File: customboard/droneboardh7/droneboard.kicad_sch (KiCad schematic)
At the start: 62 parts, among them J1 Conn_01x04, J10 Conn_01x03_Pin, J2 Conn_01x04, J3 Conn_01x05_Pin, J4 Conn_01x02_Pin, J5 USB_C_Receptacle_USB2.0_16P, J6 Conn_01x04, SW1 SW_Push, SW2 SW_Push, U1 AP62300Z6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

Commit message: stuff
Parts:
- removed J3: Conn_01x05_Pin, Connector_PinHeader_2.00mm:PinHeader_1x05_P2.00mm_Vertical, symbol Connector_Generic:Conn_01x05
- removed J4: Conn_01x02_Pin, Connector_PinHeader_2.54mm:PinHeader_1x02_P2.54mm_Vertical, symbol Connector_Generic:Conn_01x02
- removed R12, R2: 10K, Resistor_SMD:R_0201_0603Metric, symbol Device:R
- added J3, J4: Conn_01x08_MountingPin, Connector_JST:JST_SH_SM08B-SRSS-TB_1x08-1MP_P1.00mm_Horizontal, symbol Connector_Generic_MountingPin:Conn_01x08_MountingPin
- added Q1: DMN2056U, Package_TO_SOT_SMD:SOT-23, symbol Transistor_FET:DMN2056U
- J1, J2, J6: footprint Custom:PinHeaderWide4x -> Connector_JST:JST_SH_SM04B-SRSS-TB_1x04-1MP_P1.00mm_Horizontal; symbol Connector_Generic:Conn_01x04 -> Connector_Generic_MountingPin:Conn_01x04_MountingPin
- SW1, SW2: footprint Button_Switch_THT:SW_PUSH_1P1T_6x3.5mm_H4.3_APEM_MJTP1243 -> Button_Switch_SMD:SW_Push_1P1T-SH_NO_CK_KMR2xxG; symbol Switch:SW_Push -> Switch:SW_Push_Shielded
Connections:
- net 12V: now also J3.1 (Pin_1), J4.2 (Pin_2)
- net GND: now also J1.MP (MountPin), J2.MP (MountPin), J6.MP (MountPin), R1.2, SW1.SH (B), SW2.SH (B), J3.2 (Pin_2), J3.MP (MountPin), J4.1 (Pin_1), J4.MP (MountPin), Q1.2 (S); no longer J2.2 (Pin_2)
- net MOTOR0: now also J3.5 (Pin_5), J4.5 (Pin_5)
- net MOTOR1: now also J3.6 (Pin_6), J4.6 (Pin_6)
- net MOTOR2: now also J3.7 (Pin_7), J4.3 (Pin_3)
- net MOTOR3: now also J3.8 (Pin_8), J4.4 (Pin_4)
- net U4RX: no longer R1.1
- net VMCU: no longer R1.2
- net VTX_PWR: now reaches U3.4 (PE5)
- net VTX_PWR: now also R1.1, Q1.1 (G)
- new net: J2.2 (Pin_2), Q1.3 (D)
- no-connect marks 62 -> 65

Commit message: stuff
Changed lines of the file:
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@@
+	(wire
+		(pts
+			(xy 50.8 80.01) (xy 63.5 80.01)
+		)
+		(stroke
+			(width 0)
+			(type default)
+		)
+	)
 	(wire
 		(pts
@@
 	)
 	(label "VMCU"
-		(at 63.5 80.01 180)
-		(effects
-			(font
-				(size 1.27 1.27)
-			)
-			(justify right bottom)
-		)
-	)
+		(at 50.8 80.01 0)
+		(effects
+			(font
+				(size 1.27 1.27)
+			)
+			(justify left bottom)
+		)
+	)

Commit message: stuff
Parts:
- C10: footprint Capacitor_SMD:C_0402_1005Metric -> Capacitor_SMD:C_0603_1608Metric
- J1, J2, J6: value Conn_01x04 -> Conn_01x04_MountingPin
- SW1, SW2: value SW_Push -> KMR221GLFS
- Y2: value CSTNE20M0V53Z000R0 -> CSTNE8M00G520000R0
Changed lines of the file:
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@@
 			)
 		)
-		(property "Value" "Conn_01x04"
+		(property "Value" "Conn_01x04_MountingPin"
 			(at 80.01 248.0055 0)
 			(effects
@@
 			)
 		)
-		(property "Value" "SW_Push"
+		(property "Value" "KMR221GLFS"
 			(at 64.77 58.42 0)
 			(effects
@@
 			)
 		)
-		(property "Footprint" "Capacitor_SMD:C_0402_1005Metric"
+		(property "Footprint" "Capacitor_SMD:C_0603_1608Metric"
 			(at 124.1552 49.53 0)
 			(effects
@@
 			)
 		)
-		(property "Value" "CSTNE20M0V53Z000R0"
+		(property "Value" "CSTNE8M00G520000R0"
 			(at 39.37 83.8199 90)
 			(effects
@@
 			)
 		)
-		(property "Value" "Conn_01x04"
+		(property "Value" "Conn_01x04_MountingPin"
 			(at 116.84 249.2755 0)
 			(effects
@@
 			)
 		)
-		(property "Value" "Conn_01x04"
+		(property "Value" "Conn_01x04_MountingPin"
 			(at 49.53 248.0055 0)
 			(effects
@@
 			)
 		)
-		(property "Value" "SW_Push"
+		(property "Value" "KMR221GLFS"
 			(at 46.99 57.15 0)
 			(effects

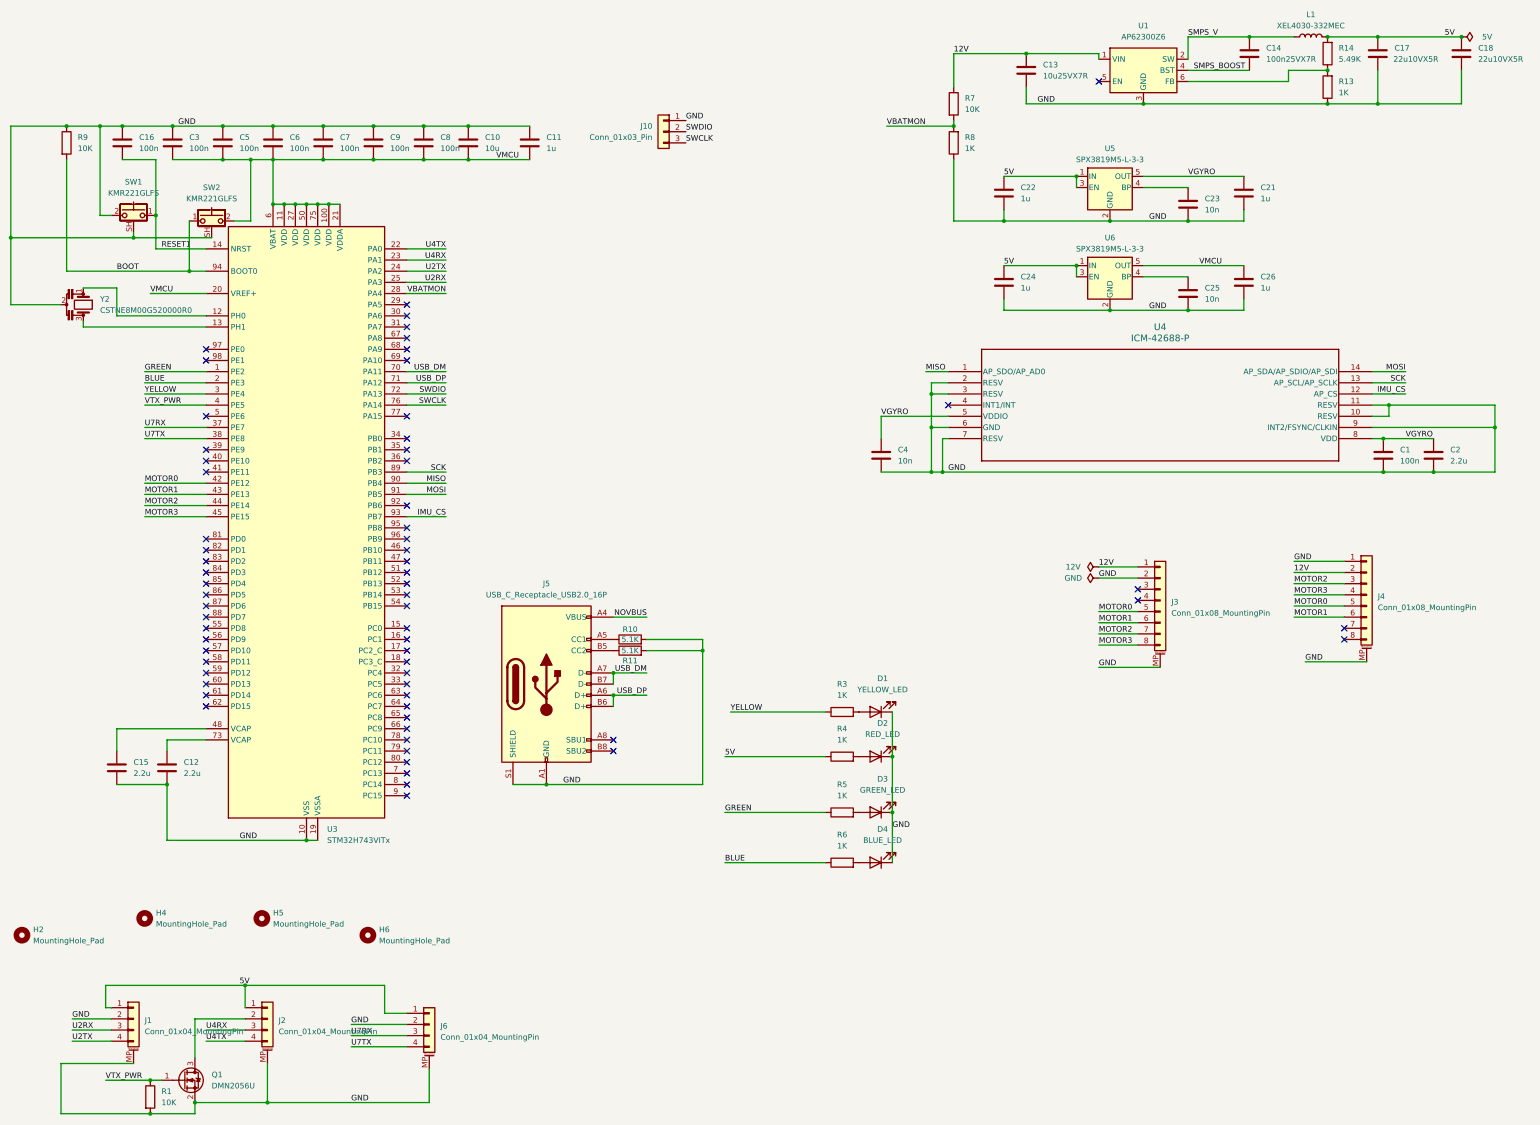
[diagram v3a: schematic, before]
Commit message: bga mcu
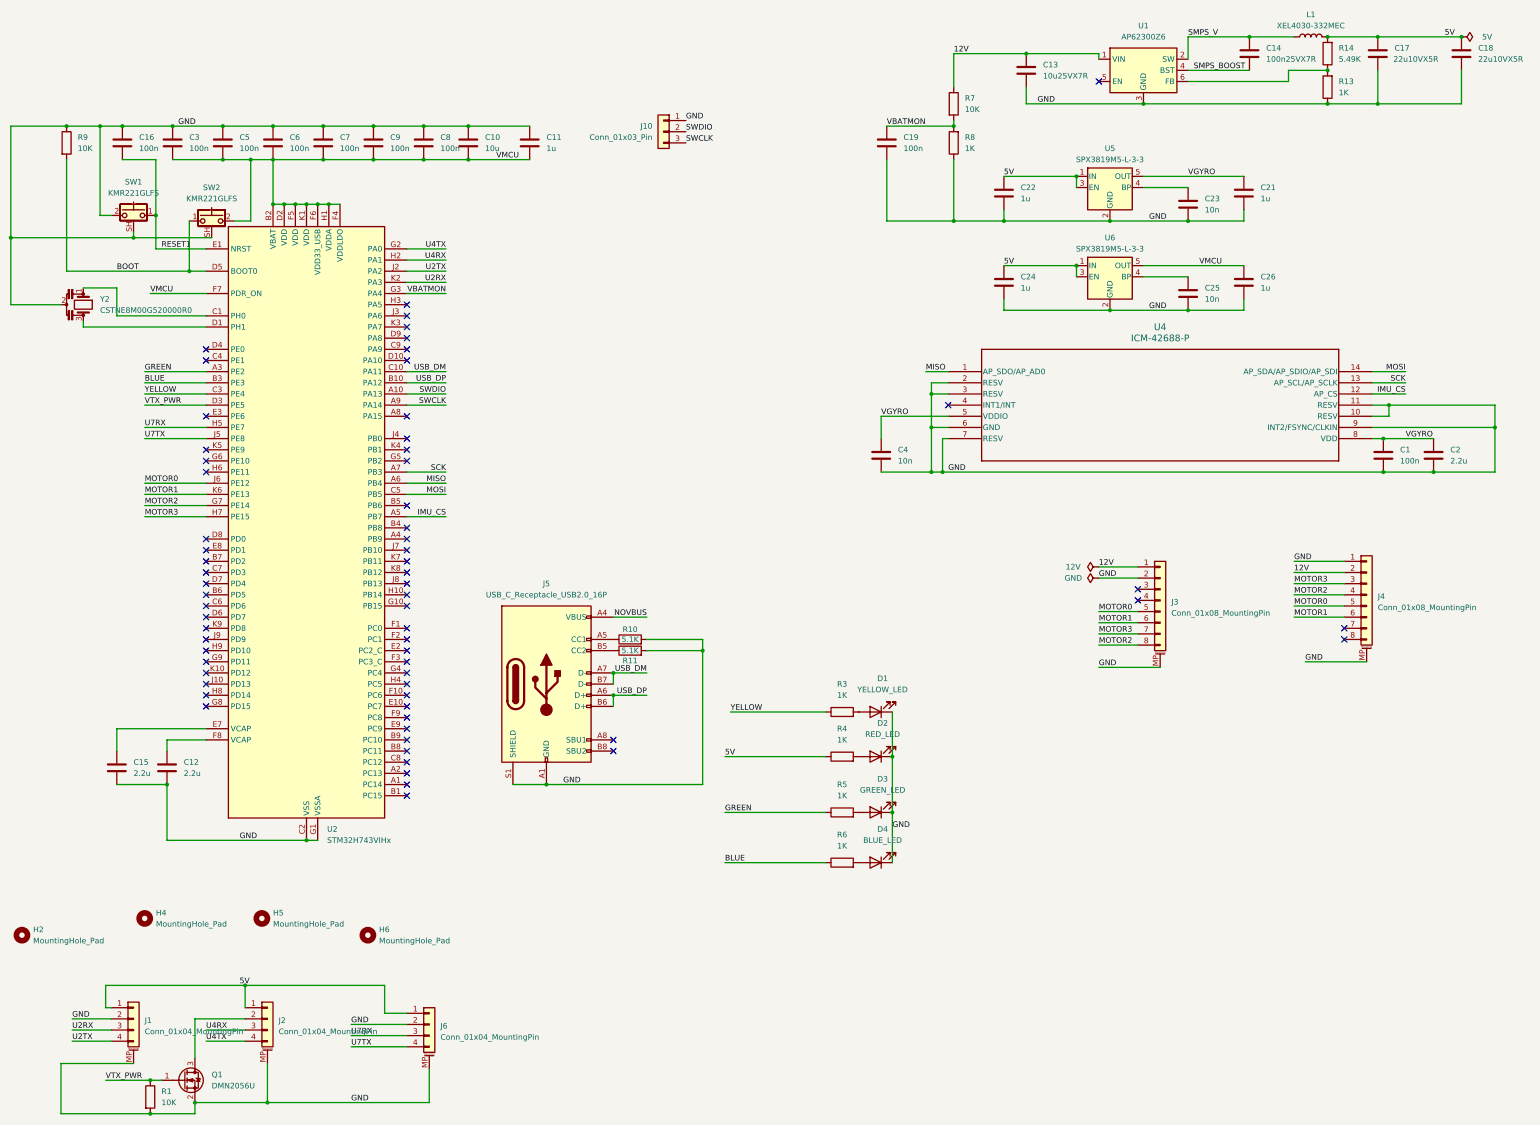
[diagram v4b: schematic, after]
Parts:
- removed U3: STM32H743VITx, Package_QFP:LQFP-100_14x14mm_P0.5mm, symbol MCU_ST_STM32H7:STM32H743VITx
- added C19: 100n, Capacitor_SMD:C_0201_0603Metric, symbol Device:C
- added U2: STM32H743VIHx, Package_BGA:TFBGA-100_8x8mm_Layout10x10_P0.8mm, symbol MCU_ST_STM32H7:STM32H743VIHx
- J10: footprint Connector_PinHeader_2.54mm:PinHeader_1x03_P2.54mm_Vertical -> Connector_PinHeader_2.00mm:PinHeader_1x03_P2.00mm_Vertical
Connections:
- net BLUE: now also U2.B3 (PE3)
- net BOOT: now also U2.D5 (BOOT0)
- net GND: now also C19.1, U2.C2 (VSS), U2.E4 (VSS), U2.E5 (VSS), U2.E6 (VSS), U2.G1 (VSSA), U2.J1 (VSS)
- net GREEN: now also U2.A3 (PE2)
- net IMU_CS: now also U2.A5 (PB7)
- net MISO: now also U2.A6 (PB4)
- net MOSI: now also U2.C5 (PB5)
- net MOTOR0: now also U2.J6 (PE12)
- net MOTOR1: now also U2.K6 (PE13)
- net MOTOR2: now also J3.8 (Pin_8), J4.4 (Pin_4), U2.G7 (PE14); no longer J3.7 (Pin_7), J4.3 (Pin_3)
- net MOTOR3: now also J3.7 (Pin_7), J4.3 (Pin_3), U2.H7 (PE15); no longer J3.8 (Pin_8), J4.4 (Pin_4)
- net RESET1: now also U2.E1 (NRST)
- net SCK: now also U2.A7 (PB3)
- net SWCLK: now also U2.A9 (PA14)
- net SWDIO: now also U2.A10 (PA13)
- net U2RX: now also U2.K2 (PA3)
- net U2TX: now also U2.J2 (PA2)
- net U4RX: now also U2.H2 (PA1)
- net U4TX: now also U2.G2 (PA0)
- net U7RX: now also U2.H5 (PE7)
- net U7TX: now also U2.J5 (PE8)
- net USB_DM: now also U2.C10 (PA11)
- net USB_DP: now also U2.B10 (PA12)
- net VBATMON: now also C19.2, U2.G3 (PA4)
- net VMCU: now also U2.B2 (VBAT), U2.D2 (VDD), U2.F4 (VDDLDO), U2.F5 (VDD), U2.F6 (VDD33_USB), U2.F7 (PDR_ON), U2.H1 (VDDA), U2.K1 (VDD)
- net VTX_PWR: now also U2.D3 (PE5)
- net YELLOW: now also U2.C3 (PE4)
- net at Y2.1: now also U2.C1 (PH0)
- net at Y2.3: now also U2.D1 (PH1)
- net at C12.1: now also U2.F8 (VCAP)
- net at C15.1: now also U2.E7 (VCAP)
